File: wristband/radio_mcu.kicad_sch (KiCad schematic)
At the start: 10 parts, among them U3 NINA-B111, U4 DWM3000

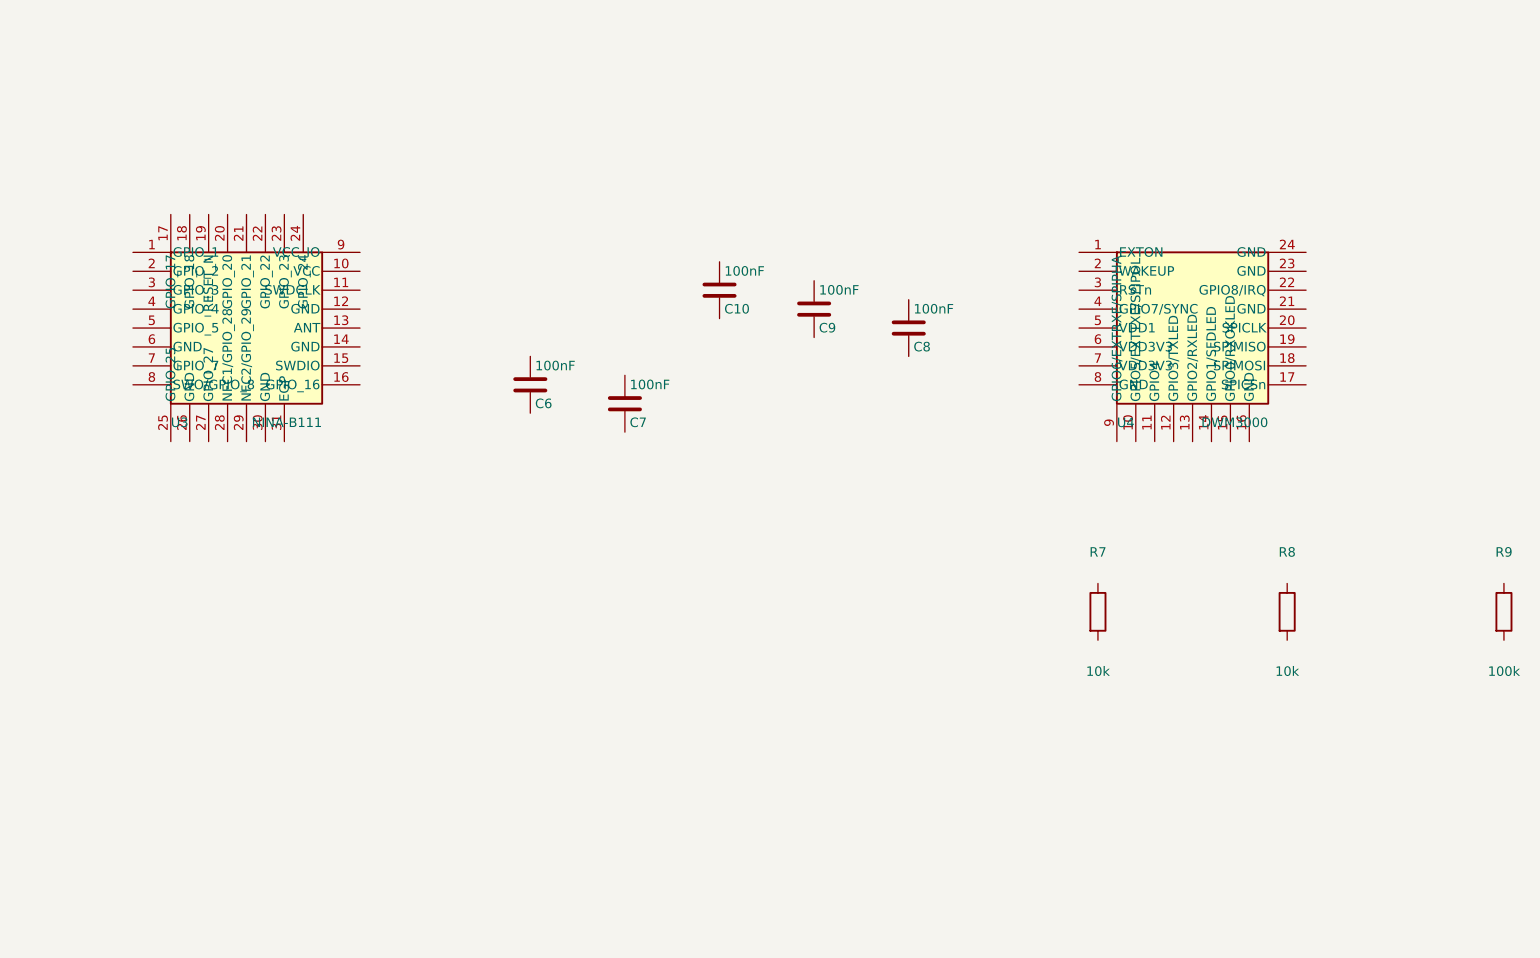
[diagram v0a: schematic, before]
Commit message: Migrate wristband to NINA-B400, wire all sheets, close six design gaps
Replaces the wristband's u-blox NINA-B111 (nRF52832) with a NINA-B400-00B
(Nordic nRF52833, Bluetooth 5.1), then follows through on everything that
change and a full schematic review surfaced.

NINA-B400 migration
- New 55-pin + EGP + EAGP symbol, transcribed from the real NINA-B40 data
  sheet UBX-19049405 R09 Table 6 and cross-checked against Figure 3 for rank
  ordering. Pin numbering validated programmatically (1-55, each exactly once).
- NINA-B4 is pin/mechanically compatible with NINA-B3, NOT NINA-B1, so the
  42-pad NINA111-42 land pattern does not carry over. No official footprint
  exists anywhere -- u-blox's own Eagle library ships only NINA111-42/112-42,
  and neither KiCad's bundled nor upstream RF_Module library has a B3/B4 part.
  NINA-B400-55_PLACEHOLDER is therefore flagged: outline, pad count and rank
  arrangement are confirmed; individual pad X/Y are derived estimates.
  MUST be replaced before fabrication.
- B400 chosen over B401/B406 for its on-module U.FL connector, which let the
  PCB-side U.FL (J2) and the untuned L/C match network (L1/C13) be deleted --
  retiring the project's only open RF-tuning risk.
- No power-design impact: abs-max VCC is 3.9 V on both modules, so the MCP1700
  LDO rationale stands. Budget 12 mA -> 15.5 mA typ; ~70.5 mA with DWM3000
  against 250 mA, ~3.5x headroom (corrects a stale "3.7x" in the docs).
- SWD pin numbers are unchanged (SWDCLK=11, SWDIO=15, RESET_N=19, SWO=8).

Antenna re-verified, part number corrected
- The specified antenna is still pre-approved for NINA-B4 (certification app
  note UBX-20037320 R05 s3.2) but ProAnt was acquired by Abracon and u-blox
  now lists it as PRO-IS-237. Same specs throughout. Order under the Abracon PN.

Six gaps closed
- Y1 + C14/C15: 32.768 kHz LFXO (Epson FC-135, Q13FC13500004). Required for
  lowest sleep current per SIM UBX-19052230 R13 s1.9; XL1/XL2 were floating,
  which Table 6 does not permit eve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
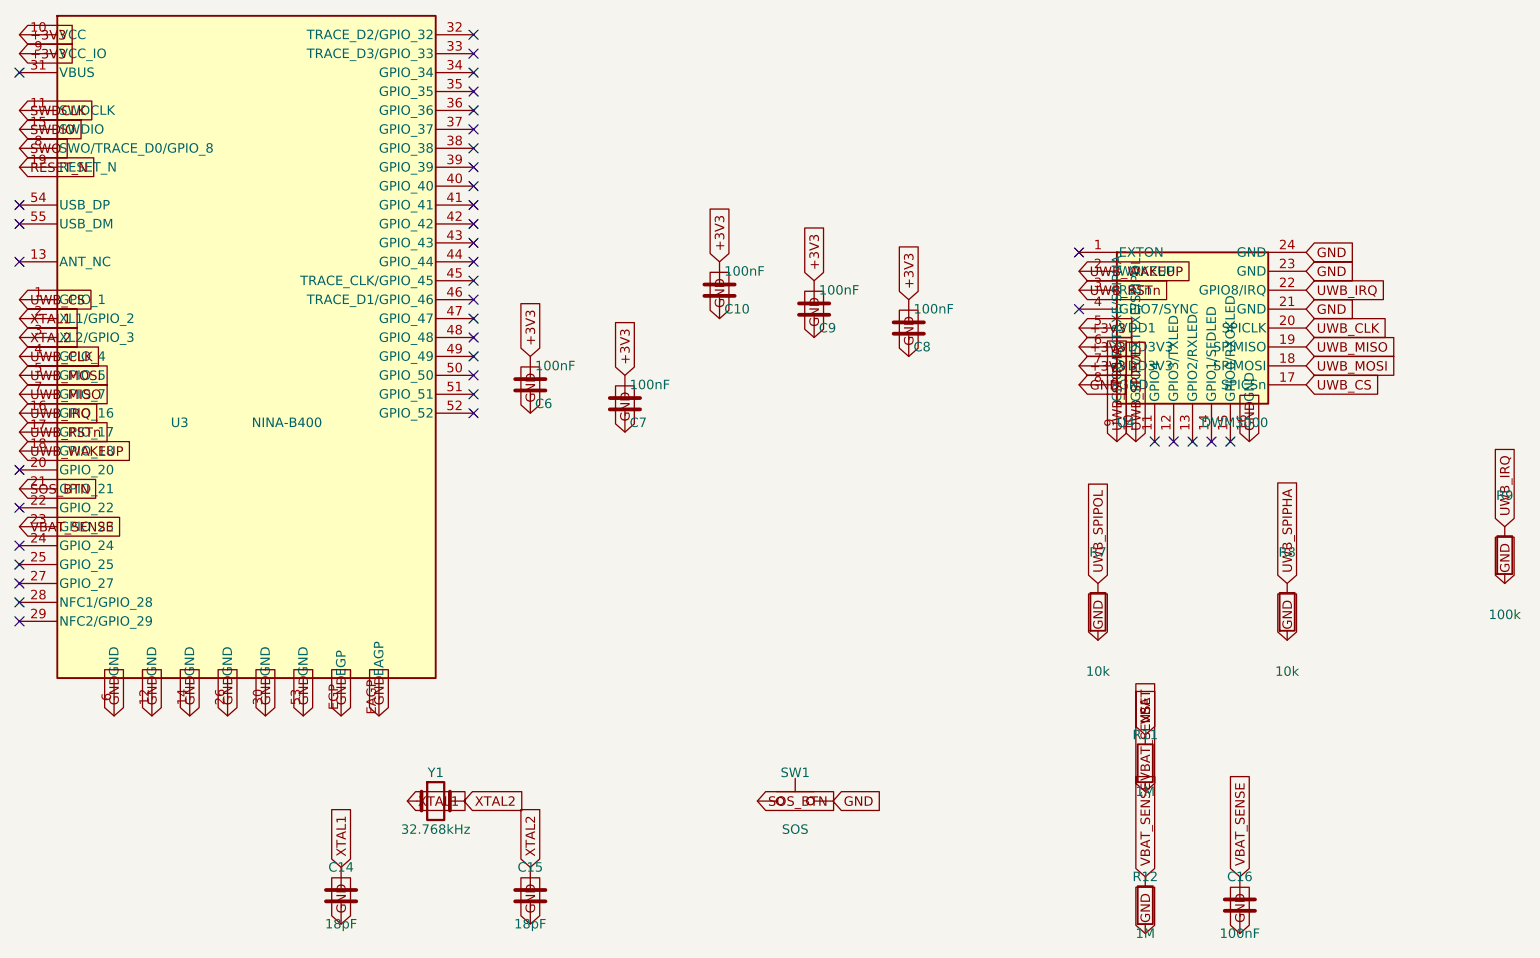
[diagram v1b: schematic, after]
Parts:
- added C14, C15: 18pF, Capacitor_SMD:C_0603_1608Metric, symbol Device:C
- added C16: 100nF, Capacitor_SMD:C_0603_1608Metric, symbol Device:C
- added R11, R12: 1M, Resistor_SMD:R_0603_1608Metric, symbol Device:R
- added SW1: SOS, Button_Switch_SMD:Panasonic_EVQPUJ_EVQPUA, symbol Switch:SW_Push
- added Y1: 32.768kHz, Crystal:Crystal_SMD_3215-2Pin_3.2x1.5mm, symbol Device:Crystal
- C10, C6, C7, C8, C9: MPN (none) -> CL10B104KB8NNNC; Manufacturer (none) -> Samsung Electro-Mechanics
- R7, R8: MPN (none) -> RC0603FR-0710KL; Manufacturer (none) -> Yageo
- R9: MPN (none) -> RC0603FR-07100KL; Manufacturer (none) -> Yageo
- U3: value NINA-B111 -> NINA-B400; footprint wristband:NINA111-42 -> wristband:NINA-B400-55_PLACEHOLDER; symbol wristband:NINA-B111 -> wristband:NINA-B400; MPN (none) -> NINA-B400-00B; Manufacturer (none) -> u-blox
- U4: MPN (none) -> DWM3000; Manufacturer (none) -> Qorvo
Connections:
- net UWB_SPIPOL: now reaches R7.1
- net UWB_SPIPOL: now also U4.10 (GPIO5/EXTTXE/SPIPOL)
- net GND: now reaches R7.2
- net GND: now also C10.2, C6.2, C7.2, C8.2, C9.2, R8.2, R9.2, U3.12 (GND), U3.14 (GND), U3.26 (GND), U3.30 (GND), U3.53 (GND), U3.6 (GND), U3.EAGP, U3.EGP, U4.16 (GND), U4.21 (GND), U4.23 (GND), U4.24 (GND), U4.8 (GND), C14.2, C15.2, C16.2, R12.2, SW1.2
- net +3V3: now reaches C6.1
- net +3V3: now also C10.1, C7.1, C8.1, C9.1, U3.10 (VCC), U3.9 (VCC_IO), U4.5 (VDD1), U4.6 (VDD3V3), U4.7 (VDD3V3)
- net UWB_SPIPHA: now reaches R8.1
- net UWB_SPIPHA: now also U4.9 (GPIO6/EXTRXE/SPIPHA)
- net UWB_IRQ: now reaches R9.1
- net UWB_IRQ: now also U3.16 (GPIO_16), U4.22 (GPIO8/IRQ)
- net UWB_CS: now reaches U3.1 (GPIO_1)
- net UWB_CS: now also U4.17 (SPICSn)
- net SWDCLK: now reaches U3.11 (SWDCLK)
- net SWDIO: now reaches U3.15 (SWDIO)
- net UWB_RSTn: now reaches U3.17 (GPIO_17)
- net UWB_RSTn: now also U4.3 (RSTn)
- net UWB_WAKEUP: now reaches U3.18 (GPIO_18)
- net UWB_WAKEUP: now also U4.2 (WAKEUP)
- net RESET_N: now reaches U3.19 (RESET_N)
- net XTAL1: now reaches U3.2 (XL1/GPIO_2)
- net XTAL1: now also C14.1, Y1.1
- net SOS_BTN: now reaches U3.21 (GPIO_21)
- net SOS_BTN: now also SW1.1
- net VBAT_SENSE: now reaches U3.23 (GPIO_23)
- net VBAT_SENSE: now also C16.1, R11.2, R12.1
- net XTAL2: now reaches U3.3 (XL2/GPIO_3)
- net XTAL2: now also C15.1, Y1.2
- net UWB_CLK: now reaches U3.4 (GPIO_4)
- net UWB_CLK: now also U4.20 (SPICLK)
- net UWB_MOSI: now reaches U3.5 (GPIO_5)
- net UWB_MOSI: now also U4.18 (SPIMOSI)
- net UWB_MISO: now reaches U3.7 (GPIO_7)
- net UWB_MISO: now also U4.19 (SPIMISO)
- net SWO: now reaches U3.8 (SWO/TRACE_D0/GPIO_8)
- new net VBAT: R11.1
- no-connect marks 0 -> 39
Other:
- moved on the sheet: R9

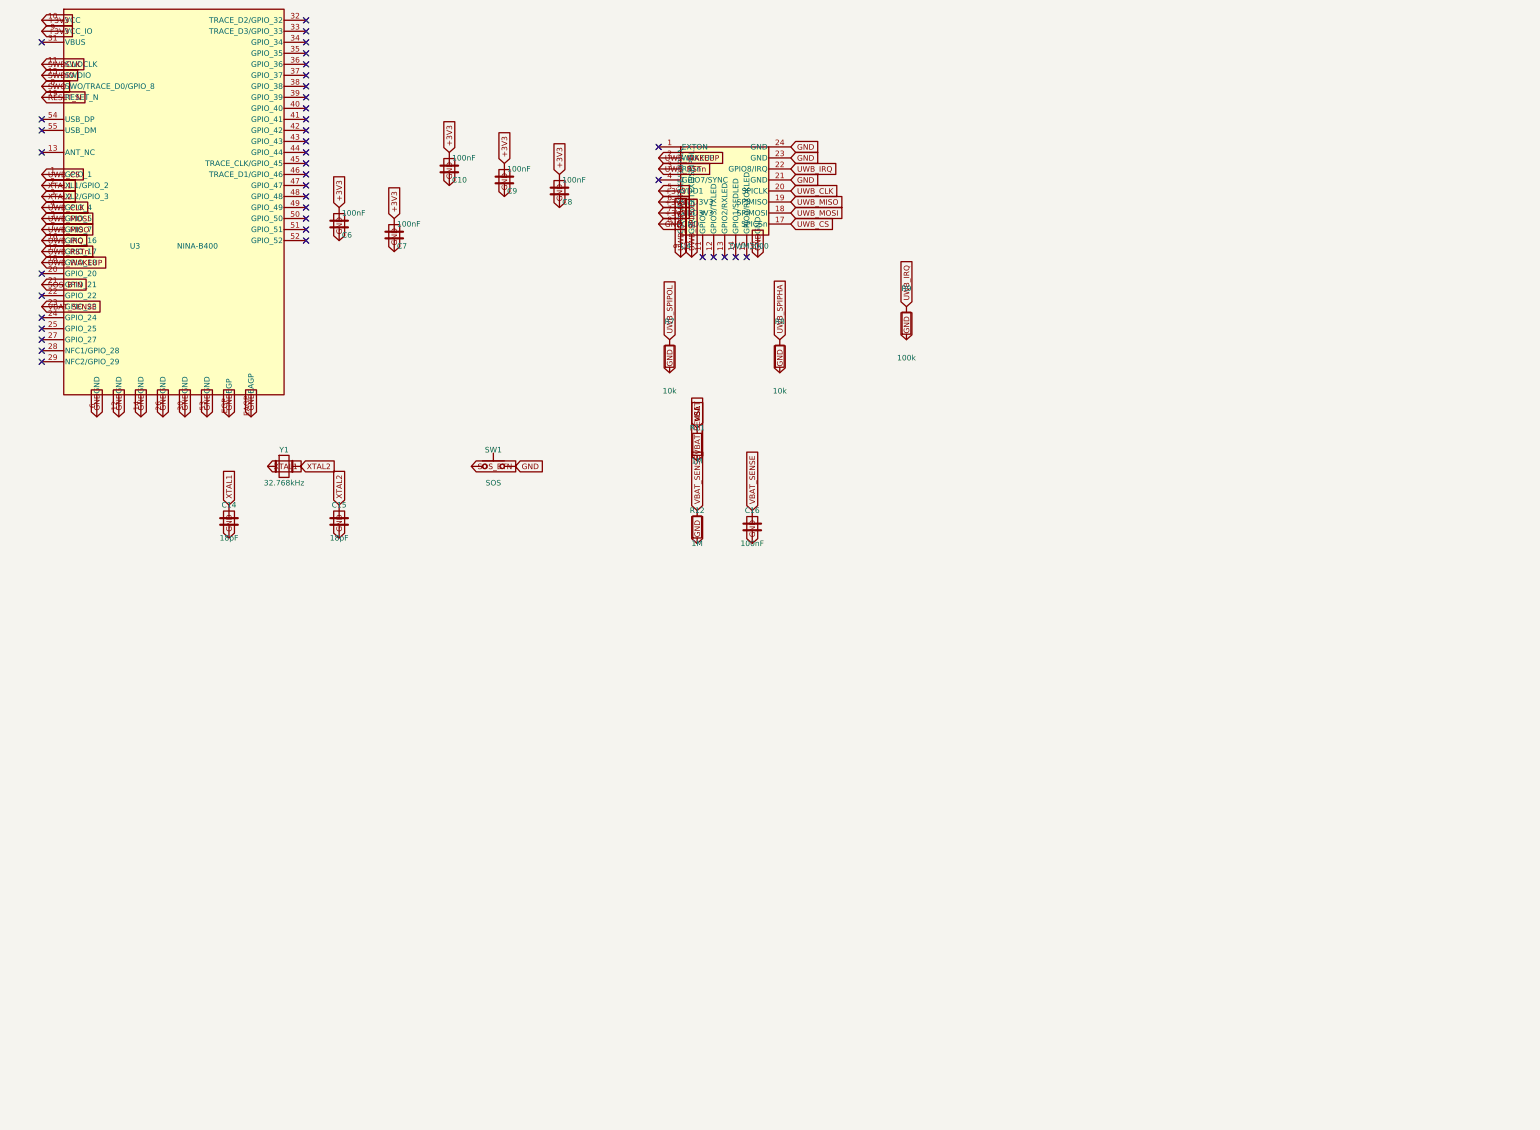
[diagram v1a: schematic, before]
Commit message: Make schematics readable: wire stubs, A3 reflow, DWM3000 symbol redraw
Connectivity is unchanged -- verified by diffing the exported netlist against
the previous commit: 34 nets, identical pin membership on every one. This is
presentation only.

The problem was pre-existing, not new. Labels were placed exactly on the pin
endpoint, so label text printed on top of the symbol's own pin name (+3V3
stamped over VCC, UWB_CS over GPIO_1). power_bms had it on U1/U2/Q2 as well;
it only became obvious when the convention was scaled onto a 55-pin part.
Every label now sits at the end of a short wire stub pointing away from the
body, which is the standard KiCad idiom.

DWM3000 symbol redrawn (shared/symbols/)
- The old symbol was a 20mm square carrying pin names like GPIO0/RXOKLED drawn
  vertically along the bottom edge, where they collided with each other inside
  the symbol. No amount of label placement fixes that.
- Now 56 x 41mm, functionally grouped: power/ground/control left, SPI/GPIO
  right, no bottom-edge pins. All 24 pins and every property preserved.
- Checked the blast radius before touching it: bay-station is entirely unwired
  (0 wires, 0 labels on every sheet), so nothing was orphaned. Its cached copy
  is refreshed here and its netlist still exports cleanly at 75 components.

Layout
- radio_mcu and power_bms moved to A3 and reflowed into functional blocks;
  42 symbols repositioned.
- 38 annotations added, carrying the datasheet citations and reasoning that
  previously lived only in the markdown -- LFXO load-cap derivation, the
  ~2.1uA battery-divider tradeoff, why DW01A's GND sits on CELL_N, the LDO
  headroom budget, and the unchanged-from-NINA-B111 SWD pin numbers.

Verification
- Wrote a text-collision checker rather than eyeballing it. It caught two
  classes of bug: duplicated annotations (strip() cleared labels and wires but
  not text, so a second pass layered notes over old ones) and doubled labels on
  stacked same-net pins (USB-C J1 A9/B9, A12/B12;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
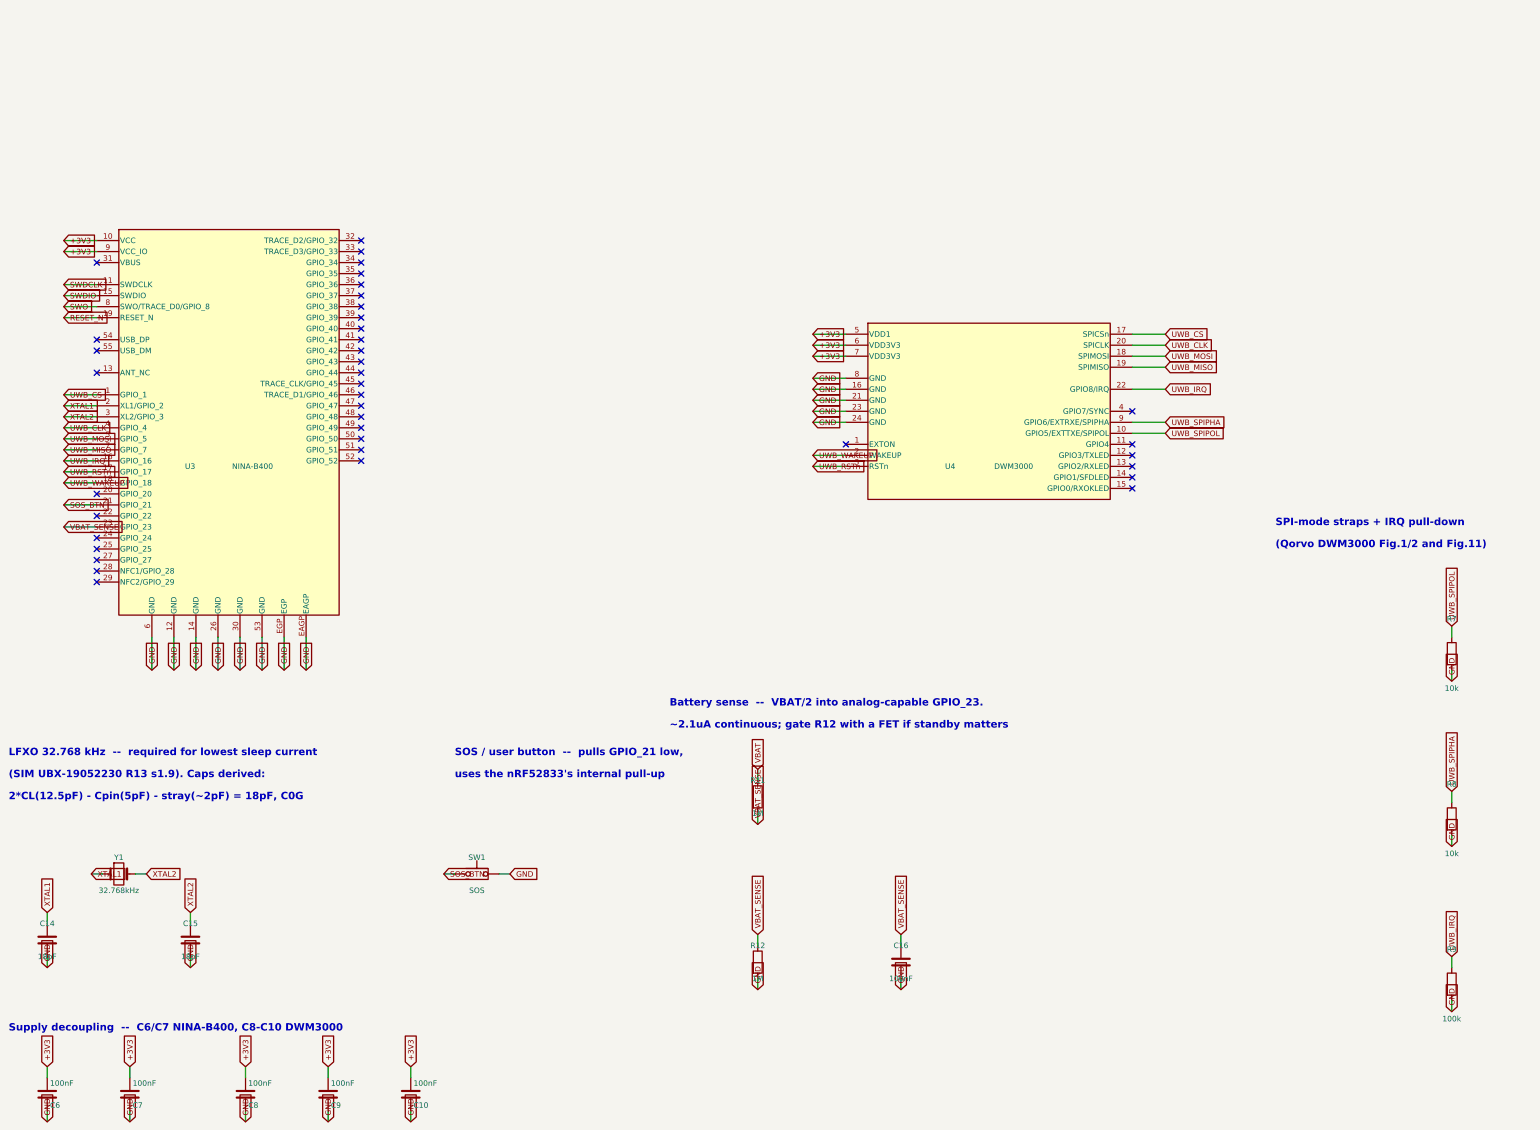
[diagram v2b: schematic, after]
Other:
- note added: "(Qorvo DWM3000 Fig.1/2 and Fig.11)"
- note added: "(SIM UBX-19052230 R13 s1.9). Caps derived:"
- note added: "2*CL(12.5pF) - Cpin(5pF) - stray(~2pF) = 18pF, C0G"
- note added: "Battery sense -- VBAT/2 into analog-capable GPIO_23."
- note added: "LFXO 32.768 kHz -- required for lowest sleep current"
- note added: "SOS / user button -- pulls GPIO_21 low,"
- note added: "SPI-mode straps + IRQ pull-down"
- note added: "Supply decoupling -- C6/C7 NINA-B400, C8-C10 DWM3000"
- note added: "uses the nRF52833's internal pull-up"
- note added: "~2.1uA continuous; gate R12 with a FET if standby matters"
- moved on the sheet: C10, C14, C15, C16, C6, C7, C8, C9, R11, R12, R7, R8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
